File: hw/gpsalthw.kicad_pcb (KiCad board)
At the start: 2 copper layers, 41 parts, among them J1 serial, J2 display, J3 antenna, Q1 IRLML5203TRPBF, Q2 IRLML5203TRPBF, SW1 reset, SW2 boot, SW3 btn-up, SW4 btn-sel, SW5 btn-down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

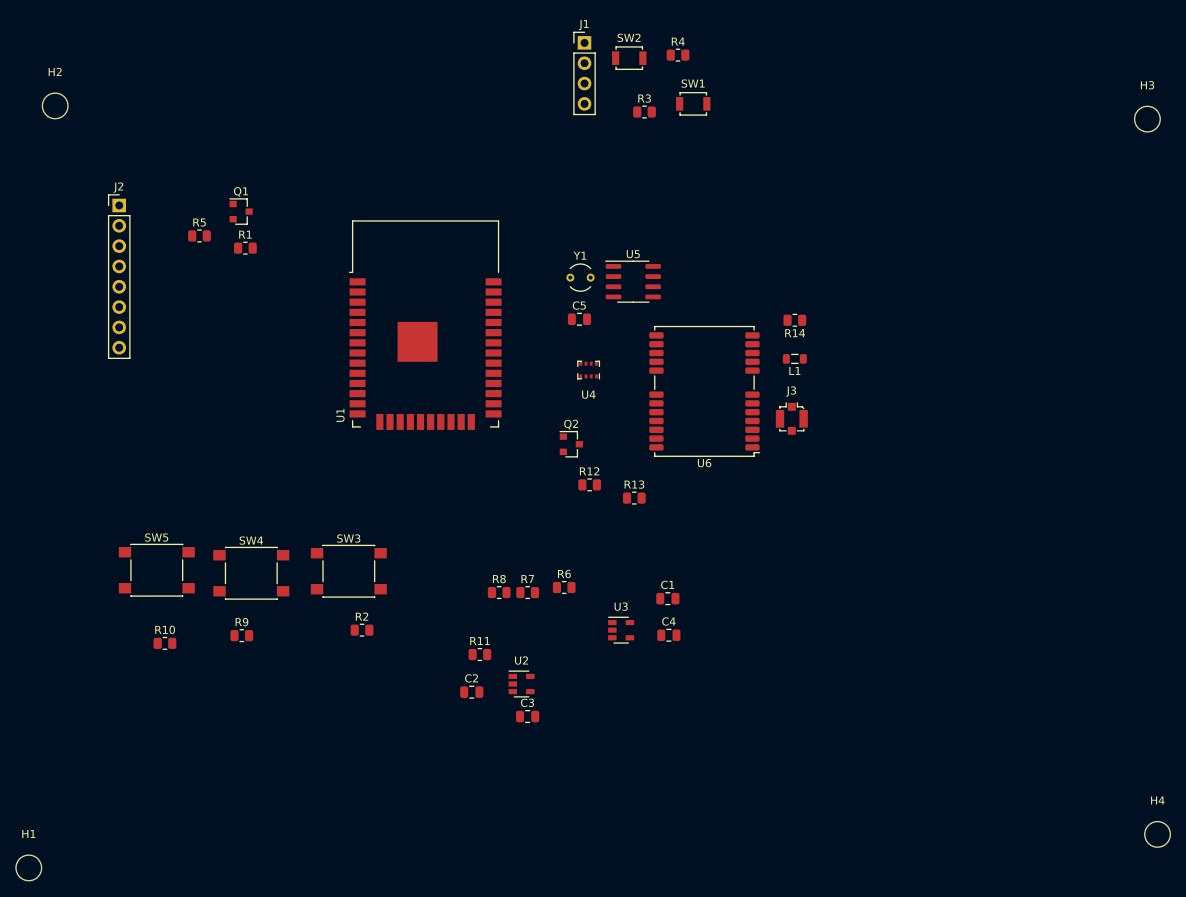
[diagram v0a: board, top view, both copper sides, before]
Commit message: плата - предварительно раскиданы элементы
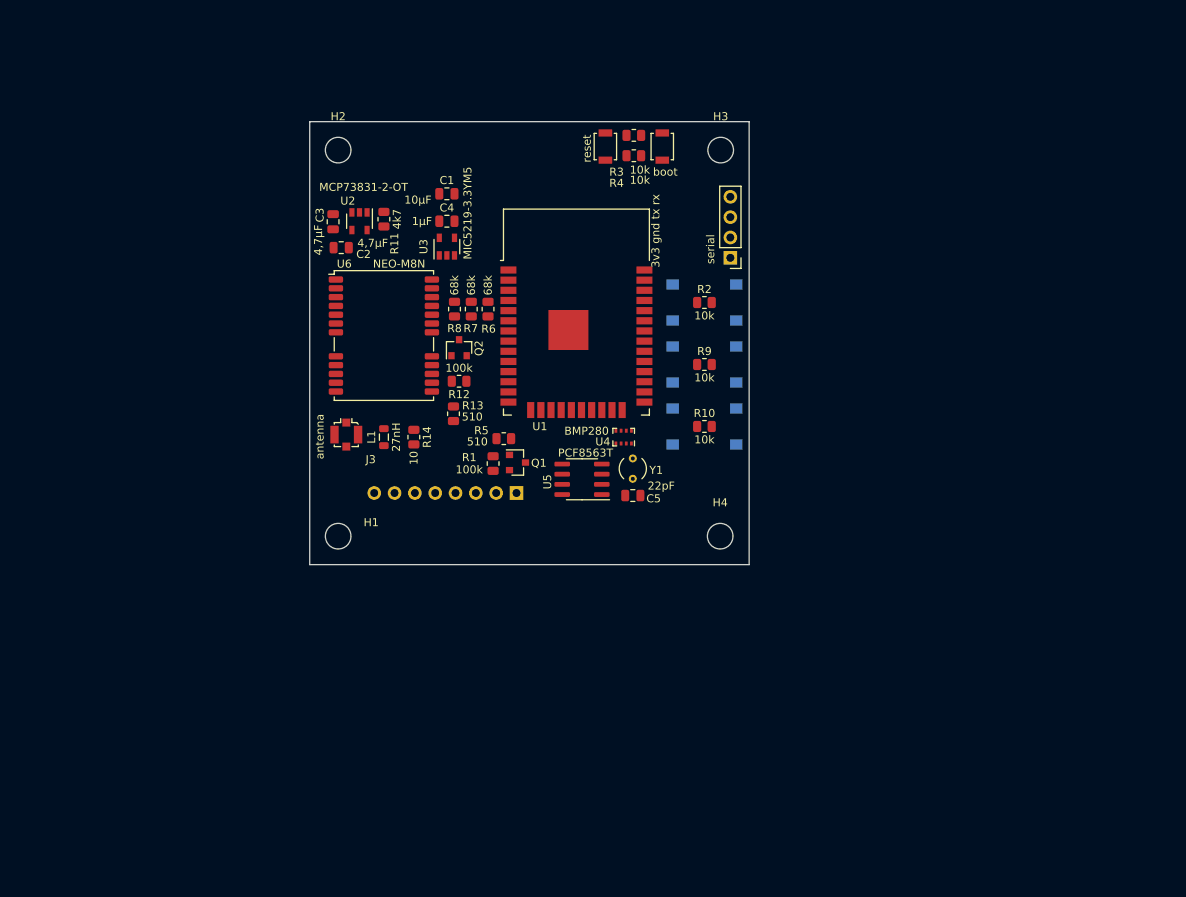
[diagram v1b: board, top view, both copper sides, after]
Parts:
- J2, SW3, SW4, SW5: moved to B.Cu
- moved R10 72.7 mm to (129.0, 81.2)
- moved SW5 70.8 mm to (129.0, 81.2), turned to 180 degrees
- moved R9 67.0 mm to (129.0, 73.5)
- moved C3 66.5 mm to (82.6, 55.6), turned to 270 degrees
- moved H4 66.2 mm to (131.0, 94.9)
- moved SW4 62.4 mm to (129.0, 73.5), turned to 180 degrees
- moved J2 61.3 mm to (105.5, 89.5), turned to 90 degrees
- moved U2 61.3 mm to (85.9, 55.6), turned to 270 degrees
- moved R2 59.2 mm to (129.0, 65.7)
- moved C4 58.7 mm to (96.8, 55.6)
- moved C2 57.9 mm to (83.6, 58.9), turned to 180 degrees
- moved C1 57.7 mm to (96.8, 52.1)
- moved H1 56.7 mm to (83.2, 94.9)
- moved R11 55.7 mm to (89.0, 55.3), turned to 90 degrees
- moved J3 55.7 mm to (84.3, 82.2)
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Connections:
- R5 pad 1: hwen -> /d-led
- U1 pad 13: Net-(U1-Pad13) -> clk-int
- U1 pad 14: Net-(U1-Pad14) -> chg-ind
- U1 pad 8: hwen -> /d-led
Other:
- board outline added: 54.9 x 55.4 mm
- board text added: "3v3 gnd tx rx"
- board text added: "Antenna"
- board text added: "led vss vdd sck sda dc rst cs"

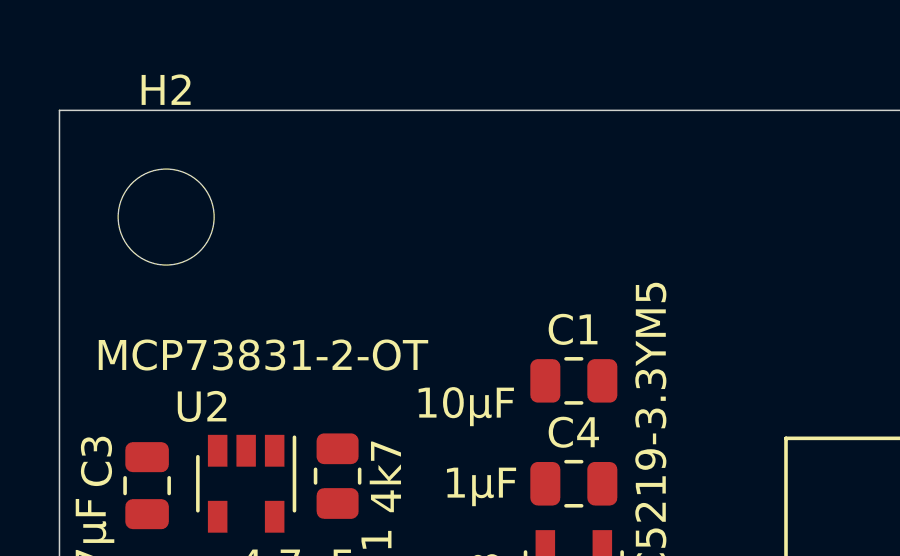
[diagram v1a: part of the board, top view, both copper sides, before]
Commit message: плата - добавлен усб-разъём
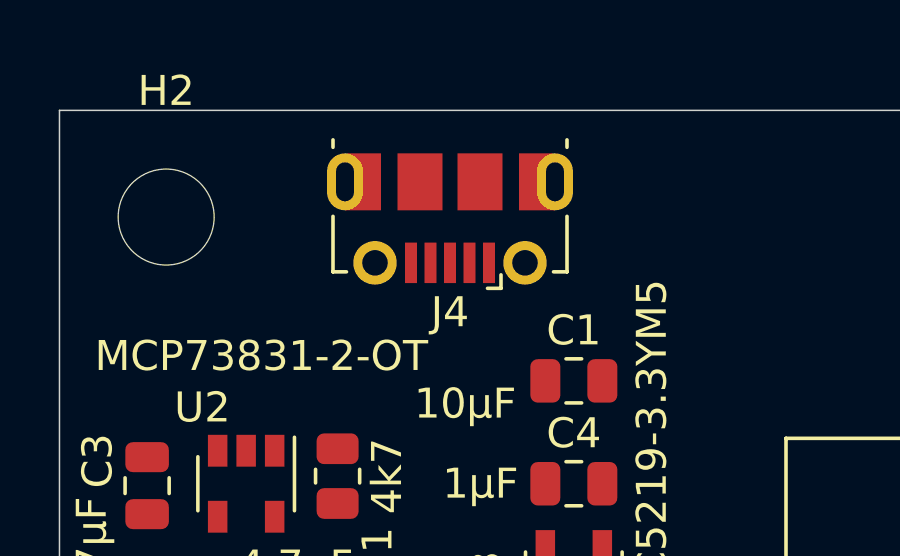
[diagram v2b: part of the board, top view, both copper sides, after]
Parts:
- added J4: USB_B_Micro, Connector_USB:USB_Micro-B_Molex-105017-0001, F.Cu at (92.7, 46.7)
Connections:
- net usb-5v renamed /usb-5v

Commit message: плата - разведены дорожки
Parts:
- moved C1 0.76 mm to (96.8, 51.4)
- moved C4 0.76 mm to (96.8, 54.8)
- moved U3 0.76 mm to (96.8, 58.0)
- moved U4 0.71 mm to (119.6, 82.4), turned to 90 degrees
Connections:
- J4 pad 6: Net-(J4-Pad6) -> GND
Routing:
- net +3V3: track 0.00 -> 173.8 mm, vias 0 -> 2
- net /spi-mosi: track 0.00 -> 60.8 mm, vias 0 -> 2
- net Net-(R4-Pad2): track 0.00 -> 54.0 mm, vias 0 -> 2
- net /spi-clk: track 0.00 -> 44.7 mm, vias 0 -> 2
- net /b-down: track 0.00 -> 43.8 mm, vias 0 -> 2
- net chg-ind: track 0.00 -> 40.7 mm, vias 0 -> 2
- net /b-sel: track 0.00 -> 37.7 mm, vias 0 -> 2
- net +BATT: track 0.00 -> 36.8 mm, vias 0 -> 2
- net /gps-rx: track 0.00 -> 36.1 mm, vias 0 -> 2
- net /gps-tx: track 0.00 -> 35.4 mm, vias 0 -> 2
- net /b-up: track 0.00 -> 31.3 mm, vias 0 -> 2
- net Net-(R3-Pad2): track 0.00 -> 30.4 mm
- net i2c-scl: track 0.00 -> 28.8 mm, vias 0 -> 2
- net /d-cs: track 0.00 -> 26.5 mm, vias 0 -> 1
- net /d-rst: track 0.00 -> 25.1 mm, vias 0 -> 1
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- added copper zone on B.Cu, net GND
- added copper zone on F.Cu, net GND
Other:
- board text added: "GPS-adv v0.1"

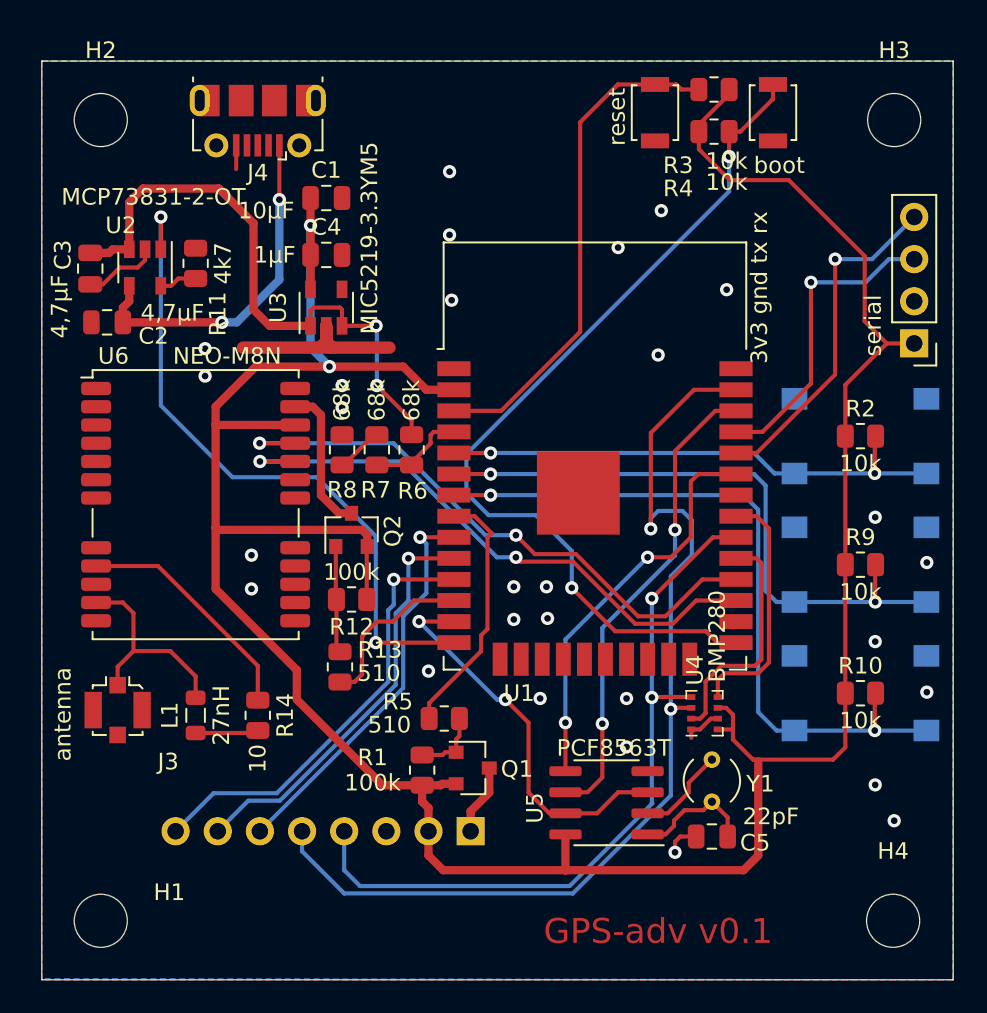
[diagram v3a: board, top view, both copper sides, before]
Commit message: плата - добавлен разъём для батареи, serial-разъём заменён на micro jst, оптимизированы некоторые дорожки (убраны лишние переходы между слоёв)
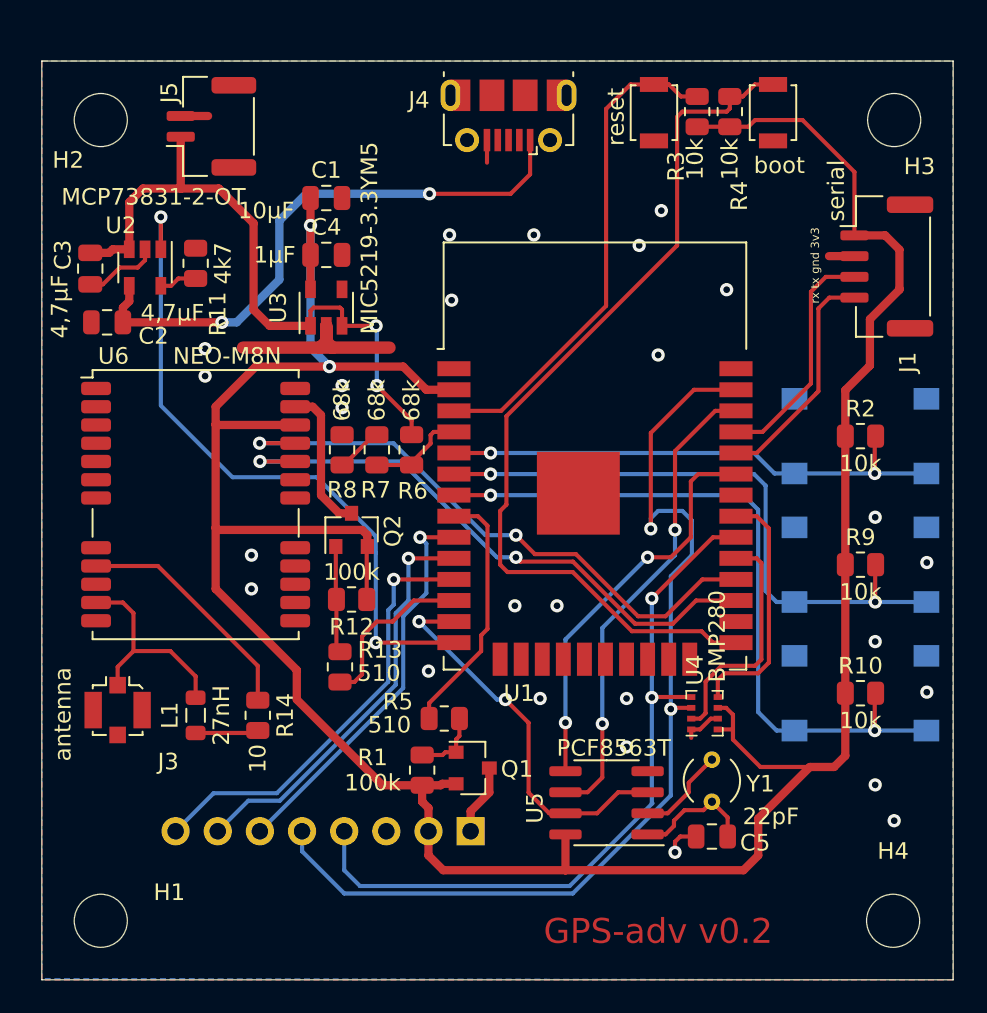
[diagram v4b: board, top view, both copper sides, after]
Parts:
- added J5: battery, Connector_JST:JST_GH_SM02B-GHS-TB_1x02-1MP_P1.25mm_Horizontal, F.Cu at (89.9, 47.1)
- J1: footprint Connector_PinHeader_2.54mm:PinHeader_1x04_P2.54mm_Vertical -> Connector_JST:JST_GH_BM04B-GHS-TBT_1x04-1MP_P1.25mm_Vertical
- moved J4 15.1 mm to (107.8, 46.4)
- moved J1 4.92 mm to (130.6, 55.5), turned to 270 degrees
- moved R3 1.68 mm to (119.2, 46.2), turned to 90 degrees
- moved R4 1.54 mm to (121.2, 46.2), turned to 90 degrees
- moved SW1 0.06 mm to (116.6, 46.2)
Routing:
- net /usb-5v: track 21.0 -> 34.6 mm
- net /RX: track 20.7 -> 14.3 mm, vias 1 -> 0
- net /TX: track 18.6 -> 14.6 mm, vias 1 -> 0
- net GND: track 22.2 -> 25.5 mm, vias 28 -> 26
- net +BATT: track 36.8 -> 39.9 mm
- net +3V3: track 173.8 -> 174.7 mm
- net Net-(R4-Pad2): track 54.0 -> 54.6 mm, vias 2 -> 0
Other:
- board text added: "GPS-adv v0.2"
- board text added: "rx tx gnd 3v3"
- board text removed: "3v3 gnd tx rx"
- board text removed: "GPS-adv v0.1"

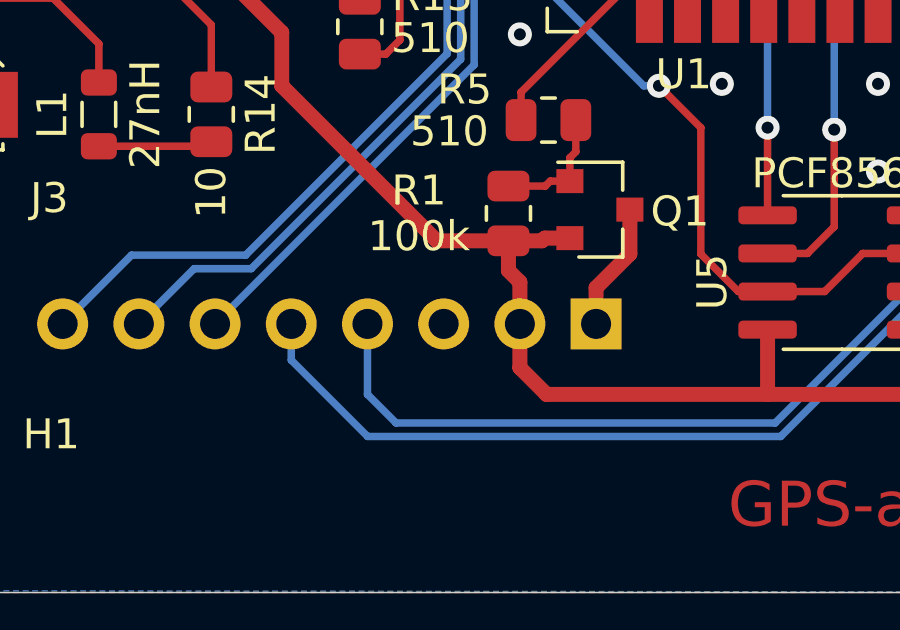
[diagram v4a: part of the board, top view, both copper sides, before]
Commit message: плата - поправлен косяк с питанием дисплея
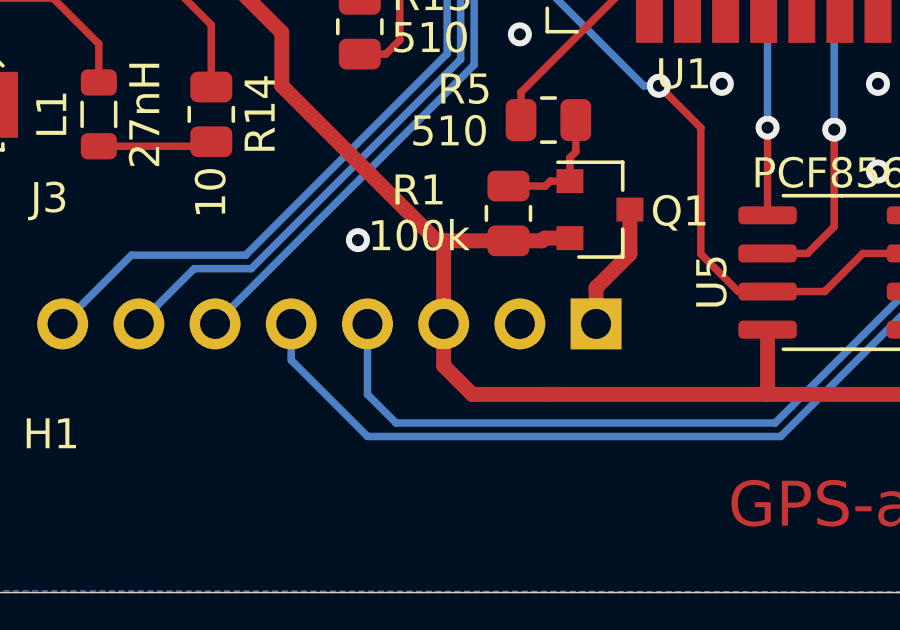
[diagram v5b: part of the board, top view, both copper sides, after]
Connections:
- J1 pad MP: GND -> (no net)
- J2 pad 2: +3V3 -> GND
- J2 pad 3: GND -> +3V3
- J5 pad MP: GND -> (no net)
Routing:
- net +3V3: track 174.7 -> 177.1 mm
- net GND: vias 26 -> 27

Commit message: плата - нормально оформлены mounting pin у раъёмов к батарее и serial
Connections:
- J1 pad MP: (no net) -> GND
- J5 pad MP: (no net) -> GND
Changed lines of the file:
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@@
       (effects (font (size 1 1) (thickness 0.15)))
     )
-    (pad MP smd roundrect (at 3.725 -1.4 270) (size 1 2.8) (layers F.Cu F.Paste F.Mask) (roundrect_rratio 0.25))
-    (pad MP smd roundrect (at -3.725 -1.4 270) (size 1 2.8) (layers F.Cu F.Paste F.Mask) (roundrect_rratio 0.25))
+    (pad MP smd roundrect (at 3.725 -1.4 270) (size 1 2.8) (layers F.Cu F.Paste F.Mask) (roundrect_rratio 0.25)
+      (net 1 GND))
+    (pad MP smd roundrect (at -3.725 -1.4 270) (size 1 2.8) (layers F.Cu F.Paste F.Mask) (roundrect_rratio 0.25)
+      (net 1 GND))
     (pad 4 smd roundrect (at 1.875 1.95 270) (size 0.6 1.7) (layers F.Cu F.Paste F.Mask) (roundrect_rratio 0.25)
       (net 5 /RX))
@@
       (effects (font (size 1 1) (thickness 0.15)))
     )
-    (pad MP smd roundrect (at 2.475 1.35 90) (size 1 2.7) (layers F.Cu F.Paste F.Mask) (roundrect_rratio 0.25))
-    (pad MP smd roundrect (at -2.475 1.35 90) (size 1 2.7) (layers F.Cu F.Paste F.Mask) (roundrect_rratio 0.25))
+    (pad MP smd roundrect (at 2.475 1.35 90) (size 1 2.7) (layers F.Cu F.Paste F.Mask) (roundrect_rratio 0.25)
+      (net 1 GND))
+    (pad MP smd roundrect (at -2.475 1.35 90) (size 1 2.7) (layers F.Cu F.Paste F.Mask) (roundrect_rratio 0.25)
+      (net 1 GND))
     (pad 2 smd roundrect (at 0.625 -1.85 90) (size 0.6 1.7) (layers F.Cu F.Paste F.Mask) (roundrect_rratio 0.25)
       (net 1 GND))
